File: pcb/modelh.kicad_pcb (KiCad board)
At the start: 2 copper layers, 150 x 38 mm, 54 parts, among them J1 Battery Conn, J2 Conn_01x20, J3 Conn_01x06, J4 Conn_01x12, J5 Conn_01x04, J6 Conn_01x04, SW1 SW_reset, U1 nice_nano, U2 74HC595, U3 74HC595, U4 74HC595

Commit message: Added testpad labels, ibom
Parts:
- removed kibuzzard-6839B7A3 (x3): G***, kibuzzard-6839B7A3
- added kibuzzard-68404910: G***, kibuzzard-68404910, F.Cu at (155.4, 48.2)
- added kibuzzard-68404916: G***, kibuzzard-68404916, F.Cu at (145.3, 57.3)
- added kibuzzard-6840491A: G***, kibuzzard-6840491A, F.Cu at (142.4, 72.0)
- TP5: value LED1 -> LED0
- TP6: value LED2 -> LED1
- TP7: value LED3 -> LED2
- moved TP1 6.01 mm to (76.8, 77.5)
- moved TP5 0.89 mm to (199.9, 61.3)
- moved TP6 0.89 mm to (199.4, 56.0)
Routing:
- net +3.3V: track 132.8 -> 269.9 mm, vias 3 -> 5
- net GND: track 54.1 -> 11.4 mm, vias 4 -> 2
- net led0r: track 38.1 -> 37.3 mm
- added copper zone on B.Cu, net GND
- removed copper zone on B.Cu, net +3.3V

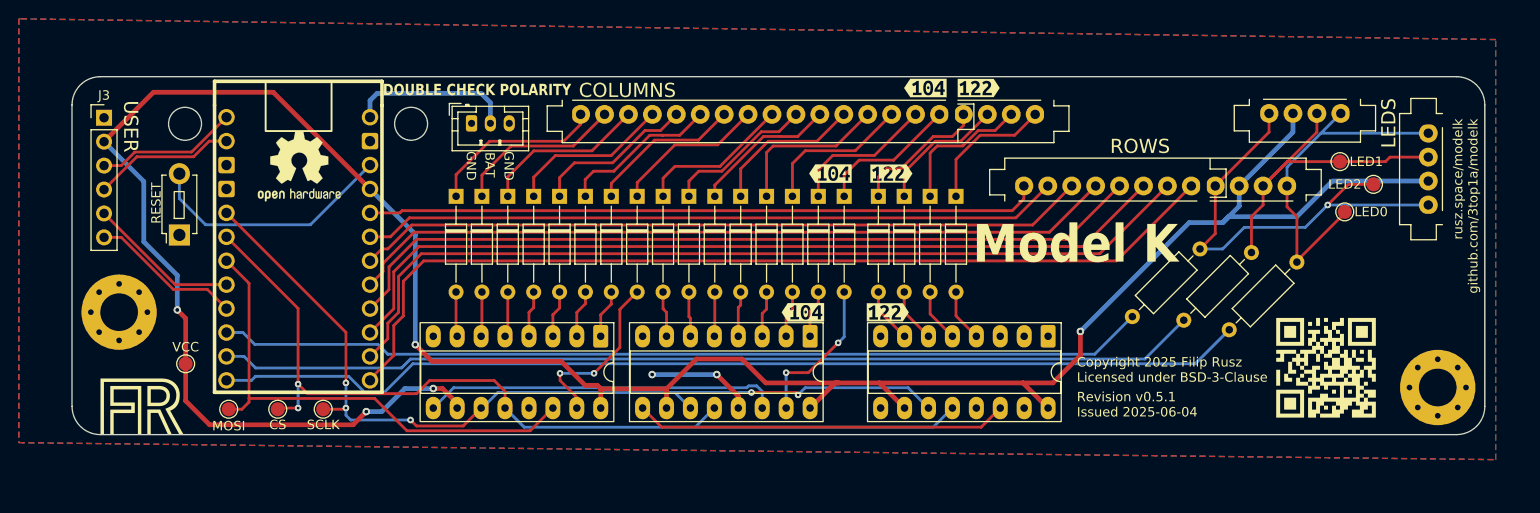
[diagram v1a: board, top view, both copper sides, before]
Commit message: Added third hole for M122
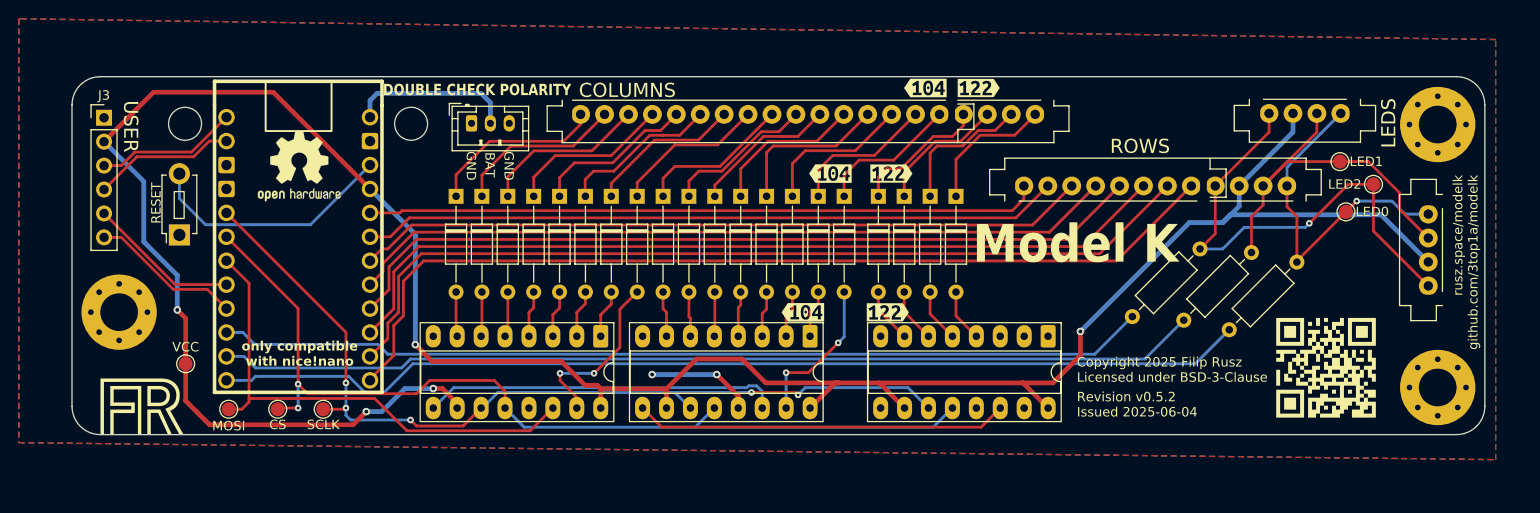
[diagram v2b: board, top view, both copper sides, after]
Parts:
- added H5: Stand, MountingHole:MountingHole_4mm_Pad_Via, F.Cu at (209.8, 52.1)
- moved J5 8.59 mm to (208.8, 65.4)
- moved TP5 0.13 mm to (200.0, 61.3)
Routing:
- net led1r: track 36.5 -> 40.6 mm
- net led2r: track 49.4 -> 51.9 mm
- net led0r: track 37.3 -> 35.5 mm, vias 0 -> 1
- net +3.3V: track 269.9 -> 270.5 mm
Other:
- board text added: "only compatible with nice!nano"

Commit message: 101 key was correct
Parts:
- removed kibuzzard-68404910: G***, kibuzzard-68404910
- removed kibuzzard-68404916: G***, kibuzzard-68404916
- removed kibuzzard-6840491A: G***, kibuzzard-6840491A
- added kibuzzard-684051F2: G***, kibuzzard-684051F2, F.Cu at (155.4, 48.2)
- added kibuzzard-684051F7: G***, kibuzzard-684051F7, F.Cu at (145.3, 57.3)
- added kibuzzard-684051FA: G***, kibuzzard-684051FA, F.Cu at (142.4, 72.0)

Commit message: Mostly stylistic changes
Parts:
- added REF**: KiCad-Logo2_5mm_SilkScreen, Symbol:KiCad-Logo2_5mm_SilkScreen, F.Cu at (88.8, 64.0)
- moved TP7 11.9 mm to (198.0, 69.2)
- moved R1 10.4 mm to (184.5, 65.3)
- moved R3 10.4 mm to (194.8, 66.7)
- moved TP6 6.31 mm to (202.1, 61.7)
- moved TP5 5.37 mm to (199.4, 56.0)
- moved TP3 4.83 mm to (86.6, 82.3)
- moved TP4 4.83 mm to (91.4, 82.3)
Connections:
- net row0 renamed /row0
- net row1 renamed /row1
- net row2 renamed /row2
- net row3 renamed /row3
- net row4 renamed /row4
- net row5 renamed /row5
- net row6 renamed /row6
- net row7 renamed /row7
- R1 pad 1: led0r -> led2r
- R3 pad 1: led2r -> led0r
- U1 pad 11: led2 -> led0
- U1 pad 13: led0 -> led2
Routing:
- net +3.3V: track 270.5 -> 239.7 mm, vias 5 -> 3
- net led2: track 98.8 -> 113.8 mm
- net GND: track 11.4 -> 24.6 mm, vias 2 -> 3
- net led2r: track 51.9 -> 43.3 mm, vias 1 -> 0
- net led0: track 110.2 -> 104.6 mm
- net col7: track 18.6 -> 23.8 mm
- net led1: track 104.2 -> 109.3 mm
- net SCLK: track 96.6 -> 101.3 mm, vias 5 -> 3
- net CS: track 100.8 -> 98.5 mm, vias 2 -> 1
- net Net-(D13-K): track 17.1 -> 15.5 mm
- net col15: track 16.3 -> 14.9 mm, vias 2 -> 0
- net MOSI: track 53.1 -> 54.0 mm, vias 0 -> 1
- net led1r: track 40.6 -> 41.3 mm
- net led0r: track 35.5 -> 35.6 mm, vias 1 -> 0

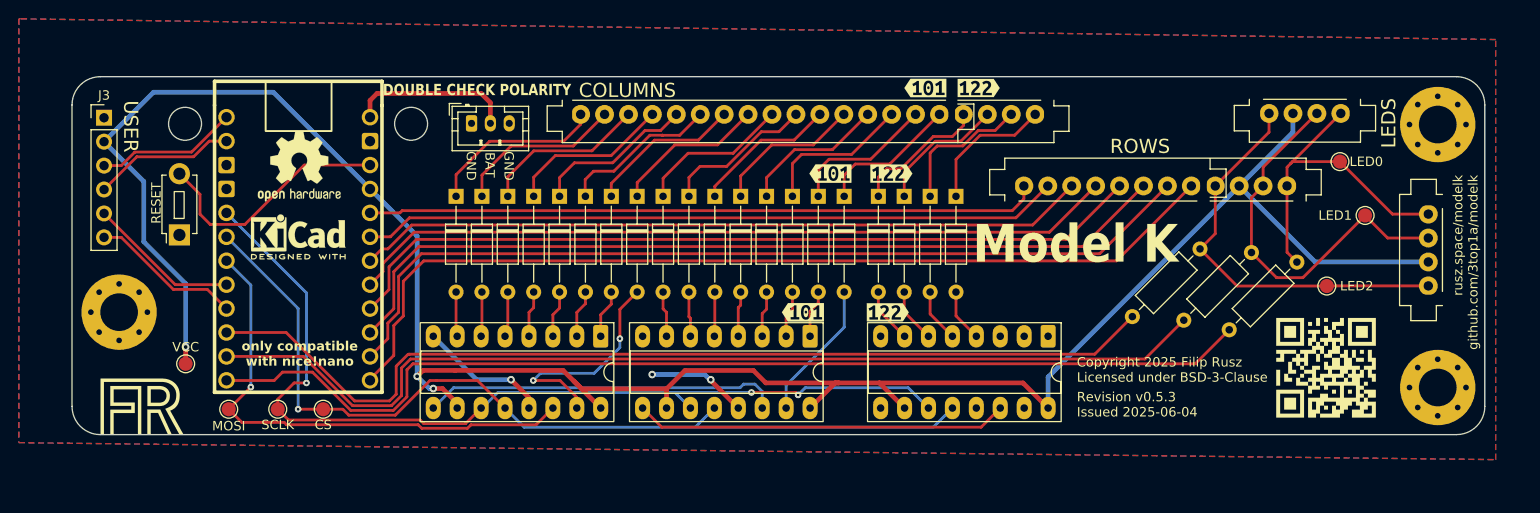
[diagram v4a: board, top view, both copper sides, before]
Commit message: Better models, added SGA font, col0 separate
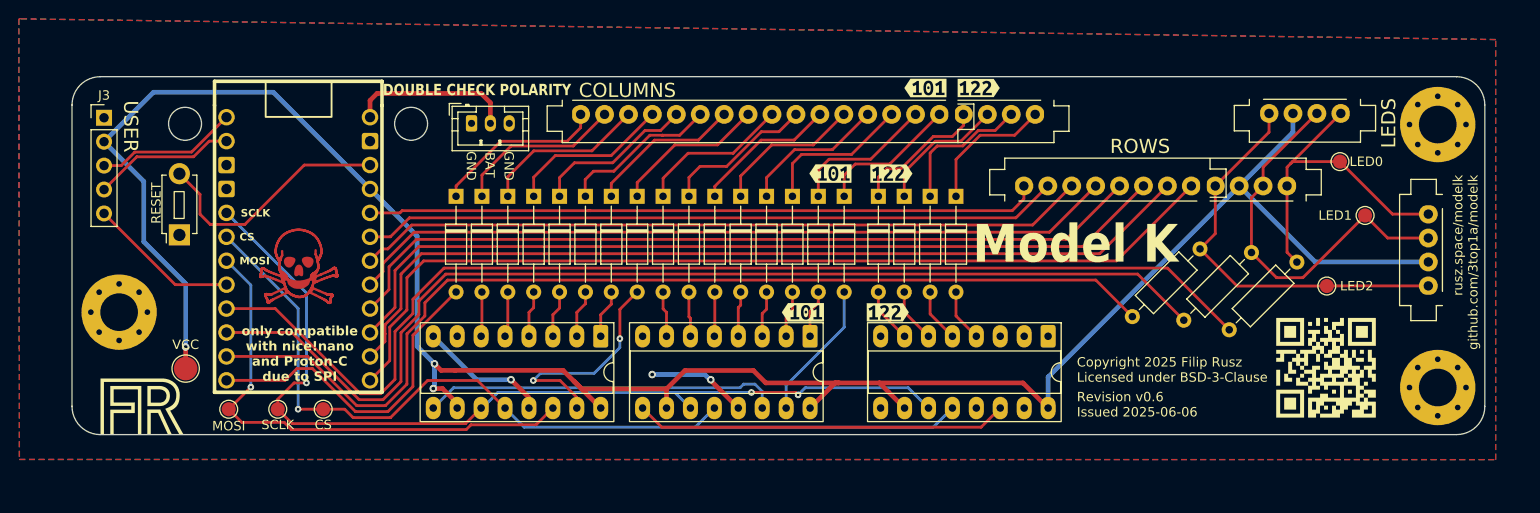
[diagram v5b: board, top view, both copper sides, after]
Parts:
- removed the REF** at (88.8, 64.0)
- added REF**: Symbol_Danger_8x8mm_Copper, Symbol:Symbol_Danger_8x8mm_Copper, F.Cu at (88.8, 67.1)
- added REF**: KiCad-Logo2_6mm_SilkScreen, Symbol:KiCad-Logo2_6mm_SilkScreen, B.Cu at (179.1, 78.7)
- J3: value Conn_01x06 -> Conn_01x05; footprint Connector_PinHeader_2.54mm:PinHeader_1x06_P2.54mm_Vertical -> Connector_PinHeader_2.54mm:PinHeader_1x05_P2.54mm_Vertical
- REF**: moved to B.Cu
- TP1: footprint Library:TestPoint -> TestPoint:TestPoint_Pad_D2.5mm
- moved REF** 111.5 mm to (198.1, 78.7), turned to 180 degrees
- moved TP1 0.51 mm to (76.8, 78.0)
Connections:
- net col1 renamed /col1
- net col10 renamed /col10
- net col11 renamed /col11
- net col12 renamed /col12
- net col13 renamed /col13
- net col14 renamed /col14
- net col15 renamed /col15
- net col16 renamed /col16
- net col17 renamed /col17
- net col18 renamed /col18
- net col19 renamed /col19
- net col2 renamed /col2
- net col3 renamed /col3
- net col4 renamed /col4
- net col5 renamed /col5
- net col6 renamed /col6
- net col7 renamed /col7
- net col8 renamed /col8
- net col9 renamed /col9
- U1 pad 10: user4 -> led2
- U1 pad 11: led0 -> led1
- U1 pad 12: led1 -> led0
- U1 pad 13: led2 -> col0
- U2 pad 7: col0 -> unconnected-(U2-QH-Pad7)
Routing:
- net col0: track 4.75 -> 35.2 mm
- net user4: track 16.1 -> 0.00 mm
- net led2: track 113.8 -> 122.3 mm
- net led1: track 109.3 -> 116.0 mm
- net led0: track 104.6 -> 109.4 mm
- net +3.3V: track 239.7 -> 237.8 mm
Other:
- board text added: "CS"
- board text added: "MOSI"
- board text added: "SCLK"
- board text added: "only compatible with nice!nano and Proton-C due to SPI"
- board text removed: "only compatible with nice!nano"

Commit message: v0.7, too much to comment
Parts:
- removed H5: Stand, MountingHole:MountingHole_4mm_Pad_Via
- removed the REF** at (179.1, 78.7)
- removed the REF** at (198.1, 78.7)
- removed TP1: VCC, TestPoint:TestPoint_Pad_D2.5mm
- removed TP2: MOSI, Library:TestPoint
- removed TP3: SCLK, Library:TestPoint
- removed TP4: CS, Library:TestPoint
- removed TP5: LED0, Library:TestPoint
- removed TP6: LED1, Library:TestPoint
- removed TP7: LED2, Library:TestPoint
- added kibuzzard-684DE304: G***, kibuzzard-684DE304, F.Cu at (209.6, 50.8)
- added kibuzzard-684DE317: G***, kibuzzard-684DE317, F.Cu at (206.5, 56.1)
- J6: value Conn_01x04 -> Conn_01x08; footprint Library:ModelH-triomate-leds4 -> Library:ModelH-triomate-rows8
- R1, R2, R3: value 100 -> 150
- U2, U3, U4: footprint Package_DIP:DIP-16_W7.62mm_Socket_LongPads -> Library:DIP-16-74HC595
- moved G*** 20.4 mm to (144.2, 44.9)
- moved R1 10.5 mm to (194.7, 62.5), turned to -90 degrees
- moved R2 9.08 mm to (198.5, 62.5), turned to -90 degrees
- moved R3 8.59 mm to (202.3, 62.5), turned to -90 degrees
- moved REF** 7.87 mm to (88.8, 59.2)
- moved J4 7.04 mm to (186.7, 56.4)
- moved J6 1.07 mm to (194.6, 51.0)
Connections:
- J6 pad 1: led2r -> /row0
- J6 pad 2: +3.3V -> /row1
- J6 pad 3: led1r -> /row2
- J6 pad 4: led0r -> /row3
- U1 pad 6: SCLK -> CS
- U1 pad 7: CS -> SCLK
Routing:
- net +3.3V: track 237.8 -> 202.3 mm, vias 3 -> 2
- net led1r: track 41.3 -> 16.2 mm
- net /row0: track 71.4 -> 94.7 mm
- net /row7: track 99.8 -> 123.1 mm
- net led0r: track 35.6 -> 12.6 mm
- net /row6: track 95.4 -> 117.8 mm
- net /row5: track 90.9 -> 113.3 mm
- net /row4: track 86.4 -> 108.8 mm
- net /row3: track 81.9 -> 104.3 mm
- net /row2: track 77.8 -> 100.2 mm
- net /row1: track 74.2 -> 96.6 mm
- net led2r: track 43.3 -> 22.6 mm
- net led0: track 109.4 -> 127.9 mm
- net led1: track 116.0 -> 132.7 mm
- net led2: track 122.3 -> 137.6 mm
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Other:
- board text added: "only compatible with nice!nano due to SPI"
- board text removed: "only compatible with nice!nano and Proton-C due to SPI"
